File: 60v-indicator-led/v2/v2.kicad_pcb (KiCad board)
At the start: 2 copper layers, 29.2 x 20.3 mm, 13 parts, among them J1 HV-IN

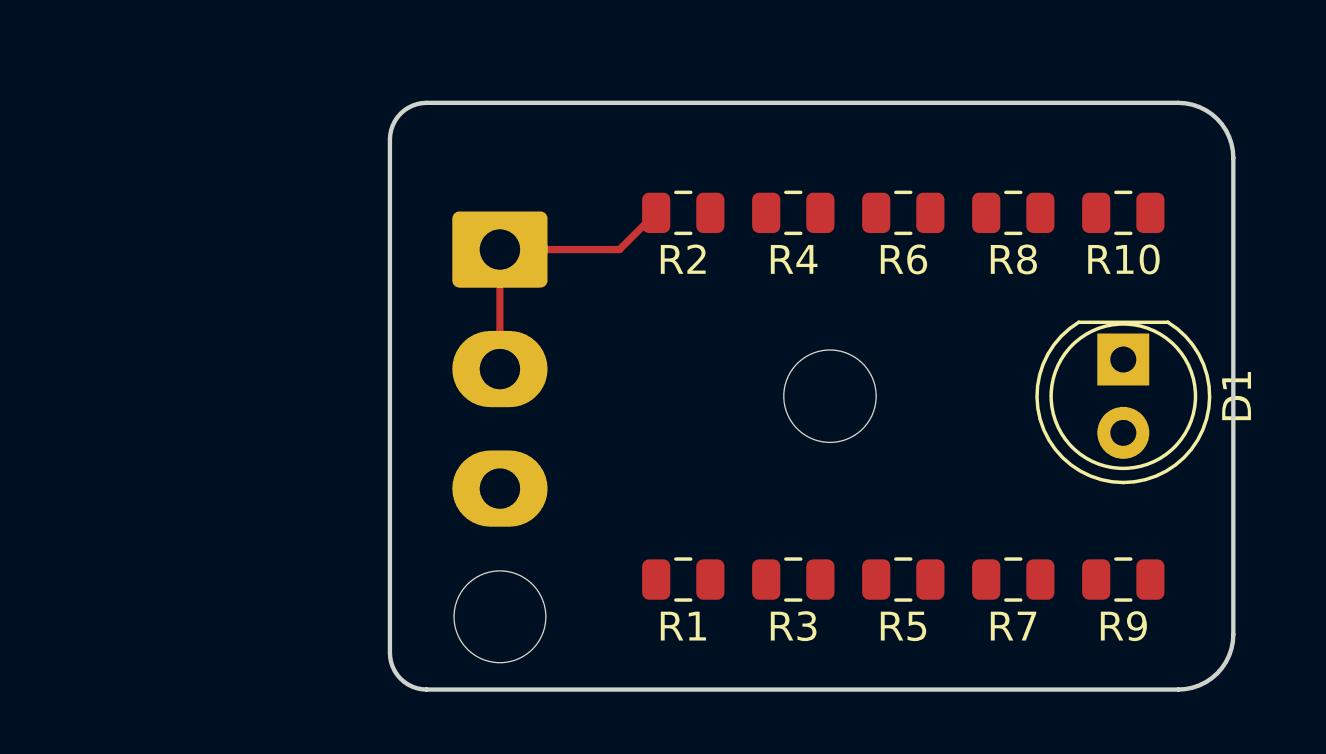
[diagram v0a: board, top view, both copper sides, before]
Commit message: Made lots of gerbers, shipped boards.
Also, re-routed interface-board to be 8/8mil minimum spacing.
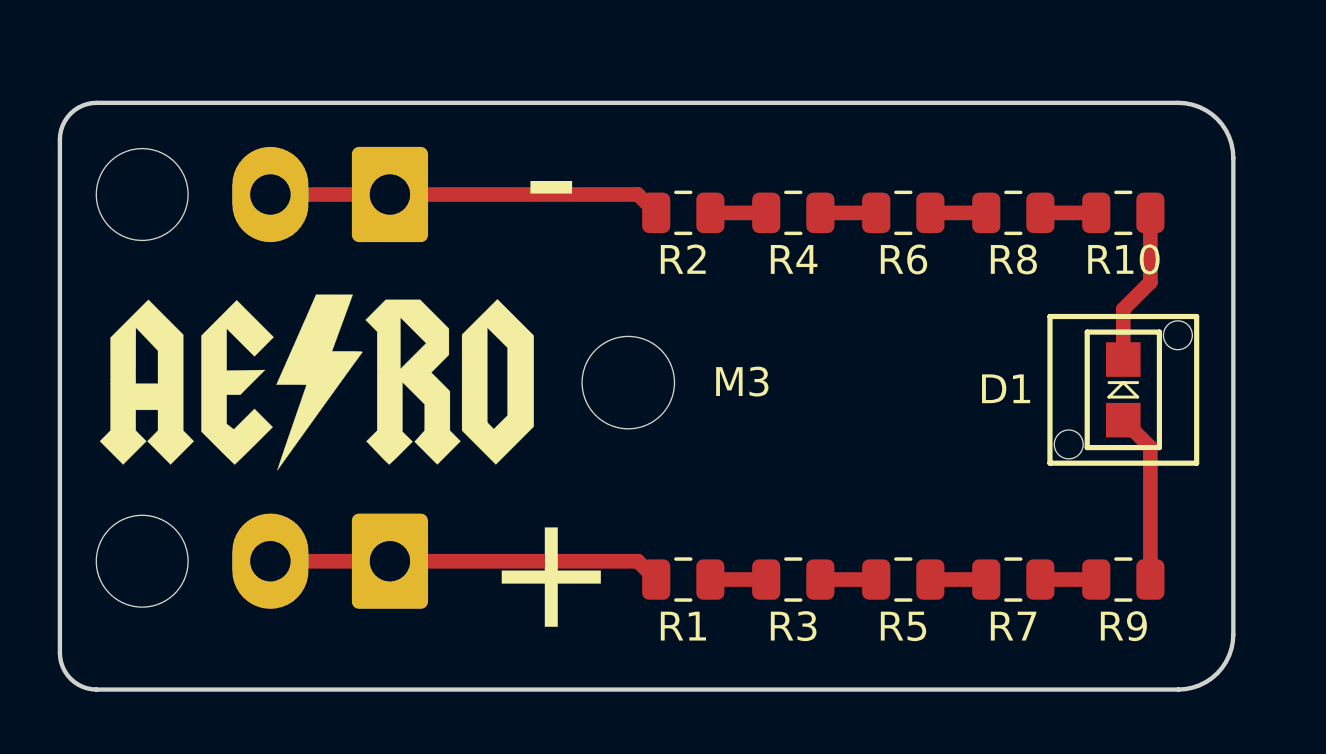
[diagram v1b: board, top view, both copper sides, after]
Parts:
- removed REF**: MountingHole_3.2mm_M3, MountingHole:MountingHole_3.2mm_M3
- added G***: LOGO, AERO_Logos:AERO_Logo_15x6mm, F.Cu at (101.6, 81.4)
- added G***: LOGO, AERO_Logos:AERO_Logo_15x6mm, B.Cu at (122.9, 77.4)
- added J2: Conn_01x02, CustomFootprints:TE_MATE-N-LOK_1-770866-x_1x02_P4.14mm_Vertical, B.Cu at (104.1, 74.9)
- added M3: MountingHole_3.2mm_M3_DIN965, MountingHole:MountingHole_3.2mm_M3_DIN965, F.Cu at (112.4, 81.4)
- D1: footprint LED_THT:LED_D5.0mm -> CustomFootprints:LPA-C011301S-x LED 0805 LIGHT PIPE SINGLE VERT SMD
- J1: value HV-IN -> Conn_01x02; footprint CustomFootprints:TE_MATE-N-LOK_1-770870-x_1x03_P4.14mm_Vertical -> CustomFootprints:TE_MATE-N-LOK_1-770866-x_1x02_P4.14mm_Vertical
- moved J1 11.4 mm to (104.1, 87.6), turned to 90 degrees
- moved D1 1.05 mm to (129.5, 81.7)
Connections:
- R1 pad 2: Net-(J1-Pad3) -> Net-(J1-Pad1)
- R2 pad 2: Net-(J1-Pad1) -> Net-(J2-Pad1)
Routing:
- net Net-(J2-Pad1): track 0.00 -> 13.6 mm
- net Net-(D1-Pad2): track 0.00 -> 5.91 mm
- net Net-(D1-Pad1): track 0.00 -> 5.47 mm
- net Net-(J1-Pad1): track 10.1 -> 13.6 mm
- net Net-(R6-Pad1): track 0.00 -> 1.94 mm
- net Net-(R5-Pad1): track 0.00 -> 1.94 mm
- net Net-(R4-Pad1): track 0.00 -> 1.94 mm
- net Net-(R3-Pad1): track 0.00 -> 1.94 mm
- net Net-(R2-Pad1): track 0.00 -> 1.94 mm
- net Net-(R1-Pad1): track 0.00 -> 1.94 mm
- net Net-(R7-Pad1): track 0.00 -> 1.93 mm
- net Net-(R10-Pad2): track 0.00 -> 1.93 mm
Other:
- board size 29.2 x 20.3 mm -> 40.6 x 20.3 mm
- net class Default: clearance 0.2 -> 0.508; trace_width 0.25 -> 0.508
- rule trace_clearance: 0.2 -> 0.508
- board text added: "+"
- board text added: "-"
- board text added: "TSV-LED Willem Hillier 3/6/2019"

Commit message: Made BOM etc for 60v-indicator-led
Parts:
- J1, J2: footprint CustomFootprints:TE_MATE-N-LOK_1-770866-x_1x02_P4.14mm_Vertical -> Connector_TE-Connectivity:TE_MATE-N-LOK_1-770866-x_1x02_P4.14mm_Vertical
- R1, R10, R2, R3, R4, R5, R6, R7, R8, R9: value 2.2k -> 1k
